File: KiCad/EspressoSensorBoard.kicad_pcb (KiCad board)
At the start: 2 copper layers, 100.4 x 22 mm, 16 parts, among them IC1 FDC1004DGSR, J1 Display, J2 MAX31855 (Temperature), J3 Screw_Terminal_01x02, J5 Pressure_Sensor, J7 Arduino_Nano_v3_Left, J8 Arduino_Nano_v3_Right, J9 Water_Level_Electrodes

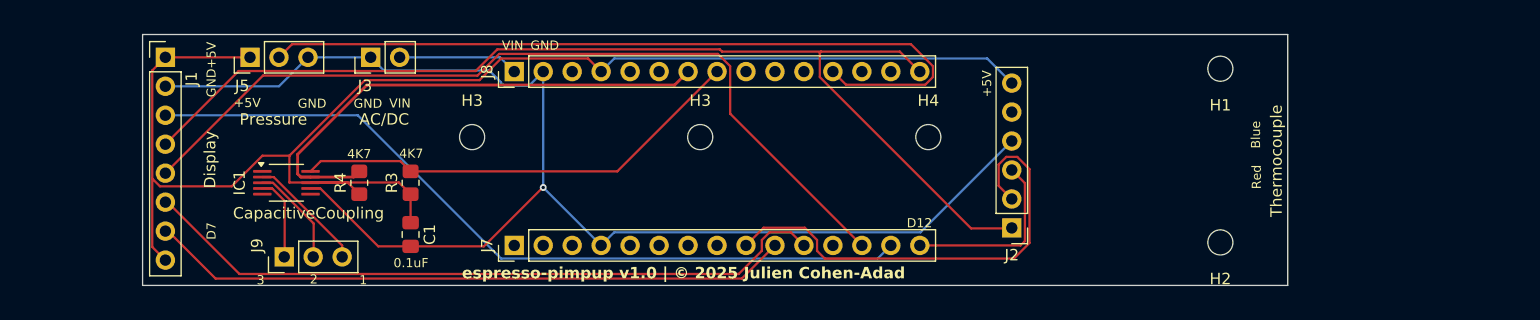
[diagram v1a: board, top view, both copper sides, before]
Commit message: Updated PCB and Arduino code
- Swapped D7 with D9 for easier routing
- Removed connection to RST on the Display (should work without it)
- Replaced connectors, notably using JST GH1.25mm for the display. https://github.com/jcohenadad/espresso-pimpup/issues/28
- Changed 3D model for Arduino. https://github.com/jcohenadad/espresso-pimpup/issues/44
- Connected pin to shielding on FDC1004. https://github.com/jcohenadad/espresso-pimpup/issues/41
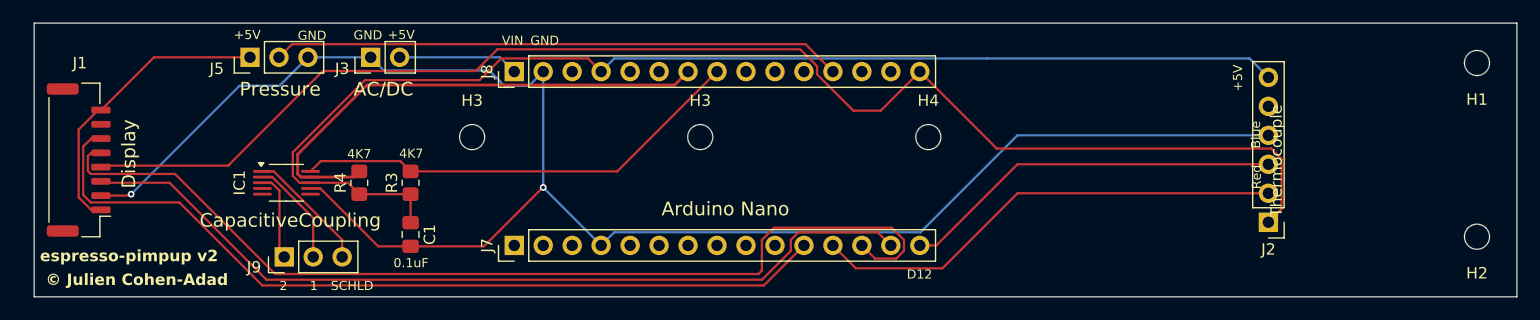
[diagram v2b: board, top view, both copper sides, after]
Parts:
- J1: value Display -> GRAPHIC DISPLAY IPS - 1.69"; footprint Connector_PinHeader_2.54mm:PinHeader_1x08_P2.54mm_Vertical -> Connector_JST:JST_GH_BM08B-GHS-TBT_1x08-1MP_P1.25mm_Vertical
- moved H1 22.5 mm to (216.0, 59.5)
- moved H2 22.5 mm to (216.0, 74.7)
- moved J2 22.5 mm to (197.7, 73.5)
- moved J1 11.8 mm to (93.4, 68.0), turned to 90 degrees
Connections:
- IC1 pad 1: unconnected-(IC1-SHLD1-Pad1) -> Net-(IC1-SHLD1)
- IC1 pad 4: Net-(IC1-CIN3) -> unconnected-(IC1-CIN3-Pad4)
- J1 pad 7: /D7 -> /RST
- J2 pad 2: /D6 -> /D9
- J7 pad 10: /D7 -> unconnected-(J7-Pin_10-Pad10)
- J7 pad 9: /D6 -> unconnected-(J7-Pin_9-Pad9)
- J9 pad 1: Net-(IC1-CIN3) -> Net-(IC1-CIN2)
- J9 pad 2: Net-(IC1-CIN2) -> Net-(IC1-CIN1)
- J9 pad 3: Net-(IC1-CIN1) -> Net-(IC1-SHLD1)
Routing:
- net /D7: track 56.7 -> 0.00 mm
- net /D9: track 0.00 -> 41.7 mm
- net /D6: track 41.1 -> 0.00 mm
- net GND: track 117.6 -> 150.0 mm, vias 1 -> 2
- net /CLK: track 95.6 -> 121.1 mm
- net /A0: track 69.1 -> 50.0 mm
- net /D12: track 16.1 -> 33.5 mm
- net /D8: track 61.4 -> 74.0 mm
- net /CS: track 74.8 -> 87.0 mm
- net Net-(IC1-SHLD1): track 0.00 -> 11.0 mm
- net Net-(IC1-CIN3): track 7.82 -> 0.00 mm
- net /D11: track 69.3 -> 75.6 mm
- net +5V: track 128.9 -> 132.1 mm
- net Net-(IC1-CIN1): track 11.0 -> 9.36 mm
- net Net-(IC1-CIN2): track 9.41 -> 7.77 mm
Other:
- board size 100.4 x 22 mm -> 130 x 24 mm
- board text added: "Arduino Nano"
- board text added: "SCHLD"
- board text added: "espresso-pimpup v2"
- board text added: "© Julien Cohen-Adad"
- board text removed: "3"
- board text removed: "D7"
- board text removed: "espresso-pimpup v1.0 | © 2025 Julien Cohen-Adad"

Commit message: Minor modifs on the Kicad PCD
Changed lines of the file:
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@@
 		(start 112.875488 69.5)
 		(end 113.725 69.5)
-		(width 0.25)
+		(width 0.2)
 		(layer "F.Cu")
 		(net 34)
@@
 		(start 145.652288 61.429084)
 		(end 118.67337 61.429084)
-		(width 0.25)
+		(width 0.2)
 		(layer "F.Cu")
 		(net 34)
@@
 		(start 146.828288 60.253084)
 		(end 145.652288 61.429084)
-		(width 0.25)
+		(width 0.2)
 		(layer "F.Cu")
 		(net 34)
@@
 		(start 112.5965 67.505954)
 		(end 112.5965 69.221012)
-		(width 0.25)
+		(width 0.2)
 		(layer "F.Cu")
 		(net 34)
@@
 		(start 117.5 69.5)
 		(end 113.725 69.5)
-		(width 0.25)
+		(width 0.2)
 		(layer "F.Cu")
 		(net 34)
@@
 		(start 118.67337 61.429084)
 		(end 112.5965 67.505954)
-		(width 0.25)
+		(width 0.2)
 		(layer "F.Cu")
 		(net 34)
@@
 		(start 112.5965 69.221012)
 		(end 112.875488 69.5)
-		(width 0.25)
+		(width 0.2)
 		(layer "F.Cu")
 		(net 34)

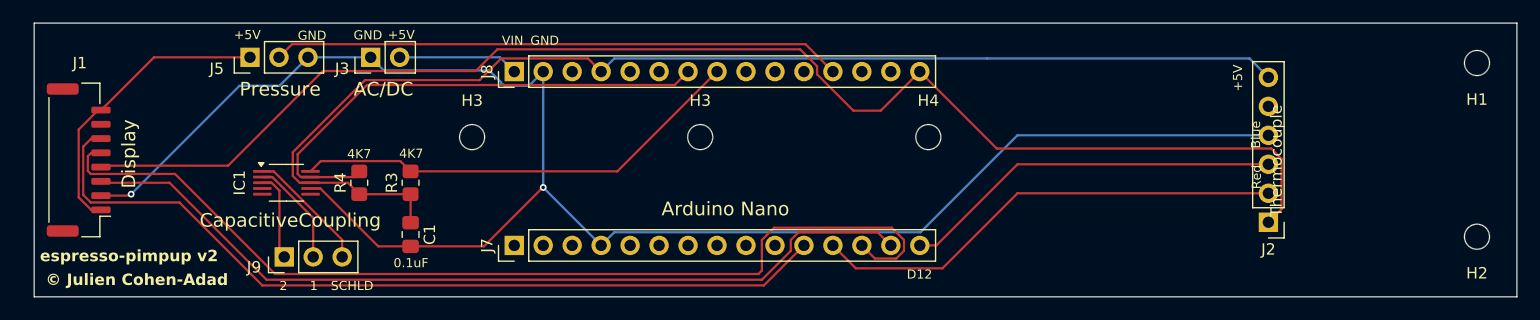
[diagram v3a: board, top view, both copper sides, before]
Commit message: Fixed missing connection
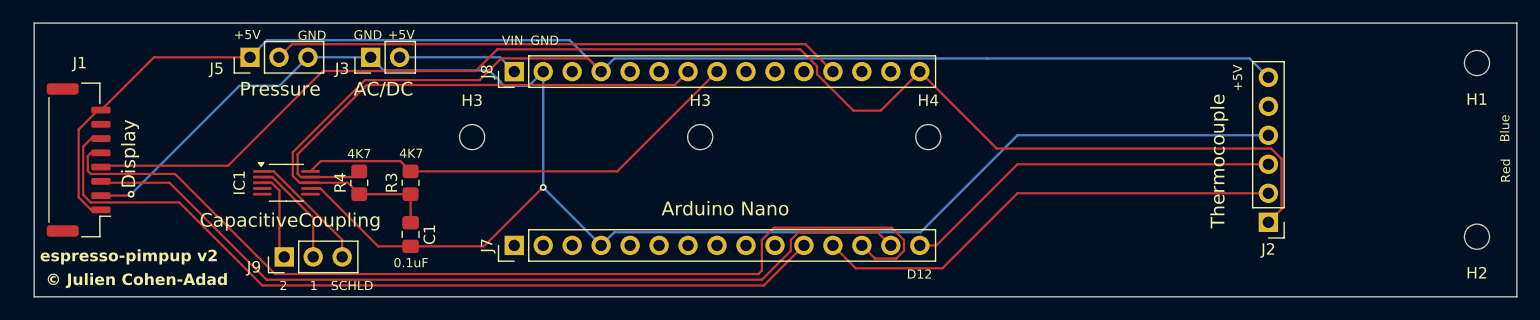
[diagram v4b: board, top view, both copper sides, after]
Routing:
- net +5V: track 132.1 -> 164.7 mm
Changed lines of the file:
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@@
 			"XgcJAQAAAHBIeykBAAAAoLItLwEAAAAwQtgrAQAAALDaBwkBAAAAcNsHCQEAAABQDf4IAQAAAHBI"
 			"eykBAAAAcEh7KQEAAABwSHspAQAAAHBIeykBAAAAMELYKwEAAABwSHspAQAAAFAN/ggBAAAA0LIt"
-			"Lw=="
+			"LwAAAAAAAAAAAAAAAAAAAAAAAAAAAAAAAAAAAAAAAAAAAAAAAAAAAAAAAAAAAAAAAAAAAAAAAAAA"
+			"AAAAAAAAAAAAAAAAAAAAAAAAAAAAAAAAAAAAAAAAAAAAAAAAAAAAAAAAAAAAAAAAAAAAAAAAAAAA"
+			"AAAAAAAAAAAAAAAAAAAAAAAAAAAAAAAAAAAAAAAAAAAAAAAAAAAAAAAAAAAAAAAAAAAAAAAAAAAA"
+			"AAAAAAAAAAAAAAAAAAAAAAAAAAAAAAAAAAAAAAAAAAAAAAAAAAAAAAAAAAAAAAAAAAAAAAAAAAAA"
+			"AAAAAAAAAAAAAAAAAAAAAAAAAAAAAAAAAAAAAAAAAAAAAAAAAAAAAAAAAAAAAAAAAAAAAAAAAAAA"
+			"AAAAAAAAAAAAAAAAAAAAAAAAAAAAAAAAAAAAAAAAAAAAAAAAAAAAAAAAAAAAAAAAAAAAAAAAAAAA"
+			"AAAAAAAAAAAAAAAAAAAAAAAAAAAAAAAAAAAAAAAAAAAAAAAAAAAAAAAAAAAAAAAAAAAAAAAAAAAA"
+			"AAAAAAAAAAAAAAAAAAAAAAAAAAAAAAAAAAAAAAAAAAAAAAAAAAAAAAAAAAAAAAAAAAAAAAAAAAAA"
+			"AAAAAAAAAAAAAAAAAAAAAAAAAAAAAAAAAAAAAAAAAAAAAAAAAAAAAAAAAAAAAAAAAAAAAAAAAAAA"
+			"AAAAAAAAAAAAAAAAAAAAAAAAAAAAAAAAAAAAAAAAAAAAAAAAAAAAAAAAAAAAAAAAAAAAAAAAAAAA"
+			"AAAAAAAAAAAAAAAAAAAAAAAAAAAAAAAAAAAAAAAAAAAAAAAAAAAAAAAAAAAAAAAAAAAAAAAAAAAA"
+			"AAAAAAAAAAAAAAAAAAAAAAAAAAAAAAAAAAAAAAAAAAAAAAAAAAAAAAAAAAAAAAAAAAAAAAAAAAAA"
+			"AAAAAAAAAAAAAAAAAAAAAAAAAAAAAAAAAAAAAAAAAAAAAAAAAAAAAAAAAAAAAAAAAAAAAAAAAAAA"
+			"AAAAAAAAAAAAAAAAAAAAAAAAAAAAAAAAAAAAAAAAAAAAAAAAAAAAAAAAAAAAAAAAAAAAAAAAAAAA"
+			"AAAAAAAAAAAAAAAAAAAAAAAAAAAAAAAAAAAAAAAAAAAAAAAAAAAAAAAAAAAAAAAAAAAAAAAAAAAA"
+			"AAAAAAAAAAAAAAAAAAAAAAAAAAAAAAAAAAAAAAAAAAAAAAAAAAAAAAAAAAAAAAAAAAAAAAAAAAAA"
+			"AAAAAAAAAAAAAAAAAAAAAAAAAAAAAAAAAAAAAAAAAAAAAAAAAAAAAAAAAAAAAAAAAAAAAAAAAAAA"
+			"AAAAAAAAAAAAAAAAAAAAAAAAAAAAAAAAAAAAAAAAAAAAAAAAAAAAAAAAAAAAAAAAAAAAAAAAAAAA"
+			"AA=="
 		)
 	)
@@
 			"AAAAUgAAAGYAAABiAAAATwAAAHoAAABEAAAAQQAAADUAAABPAAAAWgAAAGwAAABSAAAAUgAAAGsA"
 			"AABVAAAASAAAADYAAAA1AAAARQAAAGoAAABSAAAAKwAAAGkAAAAwAAAAWAAAAE0AAABxAAAARgAA"
-			"AFEAAABmAAAAbwAAAEgAAABoAAAAMQ=="
+			"AFEAAABmAAAAbwAAAEgAAABoAAAAMQAAAAAAAAAAAAAAAAAAAAAAAAAAAAAAAAAAAAAAAAAAAAAA"
+			"AAAAAAAAAAAAAAAAAAAAAAAAAAAAAAAAAAAAAAAAAAAAAAAAAAAAAAAAAAAAAAAAAAAAAAAAAAAA"
+			"AAAAAAAAAAAAAAAAAAAAAAAAAAAAAAAAAAAAAAAAAAAAAAAAAAAAAAAAAAAAAAAAAAAAAAAAAAAA"
+			"AAAAAAAAAAAAAAAAAAAAAAAAAAAAAAAAAAAAAAAAAAAAAAAAAAAAAAAAAAAAAAAAAAAAAAAAAAAA"
+			"AAAAAAAAAAAAAAAAAAAAAAAAAAAAAAAAAAAAAAAAAAAAAAAAAAAAAAAAAAAAAAAAAAAAAAAAAAAA"
+			"AAAAAAAAAAAAAAAAAAAAAAAAAAAAAAAAAAAAAAAAAAAAAAAAAAAAAAAAAAAAAAAAAAAAAAAAAAAA"
+			"AAAAAAAAAAAAAAAAAAAAAAAAAAAAAAAAAAAAAAAAAAAAAAAAAAAAAAAAAAAAAAAAAAAAAAAAAAAA"
+			"AAAAAAAAAAAAAAAAAAAAAAAAAAAAAAAAAAAAAAAAAAAAAAAAAAAAAAAAAAAAAAAAAAAAAAAAAAAA"
+			"AAAAAAAAAAAAAAAAAAAAAAAAAAAAAAAAAAAAAAAAAAAAAAAAAAAAAAAAAAAAAAAAAAAAAAAAAAAA"
+			"AAAAAAAAAAAAAAAAAAAAAAAAAAAAAAAAAAAAAAAAAAAAAAAAAAAAAAAAAAAAAAAAAAAAAAAAAAAA"
+			"AAAAAAAAAAAAAAAAAAAAAAAAAAAAAAAAAAAAAAAAAAAAAAAAAAAAAAAAAAAAAAAAAAAAAAAAAAAA"
+			"AAAAAAAAAAAAAAAAAAAAAAAAAAAAAAAAAAAAAAAAAAAAAAAAAAAAAAAAAAAAAAAAAAAAAAAAAAAA"
+			"AAAAAAAAAAAAAAAAAAAAAAAAAAAAAAAAAAAAAAAAAAAAAAAAAAAAAAAAAAAAAAAAAAAAAAAAAAAA"
+			"AAAAAAAAAAAAAAAAAAAAAAAAAAAAAAAAAAAAAAAAAAAAAAAAAAAAAAAAAAAAAAAAAAAAAAAAAAAA"
+			"AAAAAAAAAAAAAAAAAAAAAAAAAAAAAAAAAAAAAAAAAAAAAAAAAAAAAAAAAAAAAAAAAAAAAAAAAAAA"
+			"AAAAAAAAAAAAAAAAAAAAAAAAAAAAAAAAAAAAAAAAAAAAAAAAAAAAAAAAAAAAAAAAAAAAAAAAAAAA"
+			"AAAAAAAAAAAAAAAAAAAAAAAAAAAAAAAAAAAAAAAAAAAAAAAAAAAAAAAAAAAAAAAAAAAAAAAAAAAA"
+			"AAAAAAAAAAAAAAAAAAAAAAAAAAAAAAAAAAAAAAAAAAAAAAAAAAAAAAAAAAAAAAAAAAAAAAAAAAAA"
+			"AAAAAAAAAAAAAAAAAAAAAAAAAAAAAA=="
 		)
 	)
@@
 			"AAICAwADAgAA/v8AAP//AAD+/v4AxcbCAIaKhQDGycYAMjQyAHV2dwBFQUgA/AD9AAUABgD8APwA"
 			"BAAEAP0A+wD+//0ABgEFAPoA+wAEAAQA/wD/APwA/QD2+PYAoaOiAIGGhQD68/AAOlJQABAaGADW"
-			"2toAGxgcAC8qLQAfGR0AFA=="
+			"2toAGxgcAC8qLQAfGR0AFADe4eAA+v38AMjKyQAJCgkALi0tANTT0gAB//8ABAMCAOfm5gAICAkA"
+			"BAQEAAEBAAD+//4AAwUDAPL18wD9AP8A/wQCABwgHwD5+/oAAwQEAAUEBAD9+fkAAf3/AAQAAQD4"
+			"9/QABAMAAA4QDAAFBQQAAAABAPz4/gD19fgAFxgaABcUFADy6+oAGBgWAAgOCwDh4+MA8fHzAA4O"
+			"DgDr6+gA/v7+AAMEBgD//wAABQUEAPf49gD6+/oADQ0MAP8A/gDs7OwADAwLAAD+/wARERIADg0N"
+			"AOTj5QD7+vsAIyMkAAQGBwDe4uIA/wIDAAgLCwAAAwEA+v77AP4B/QABAv0AAAIAAAUHCQAFBgoA"
+			"BQYLAAcGCwAEAwYABQIDAPj29AAI/v4AW0tLAEUxQwEAAAAAAAAAAAAAAAAAAAAAAAAAAAAAAAAA"
+			"AAAAAAAAAAAAAAAAAAAAAAAAAAAAAAAAAAAAAAAAAAAAAAAAAAAAAAAAAAAAAAAAAAAAAAAAAAAA"
+			"AAAAAAAAAAAAAAAAAAAAAAAAAAAAAAAAAAAAAAAAAAAAAAAAAAAAAAAAAAAAAAAAAAAAAAAAAAAA"
+			"AAAAAAAAAAAAAAAAAAAAAAAAAAAAAAAAAAAAAAAAAAAAAAAAAAAAAAAAAAAAAQAAAAAAAAAAAAAA"
+			"AAAAAAAAAAAAAAAAAAAAAAAAAAAAAAAAAAAAAAAAAAAAAAAAAAAAAAAAAAAAAAAAAAAAAAAAAAAA"
+			"AAAAAAAAAAAAAAAAAAAAANnS2v/z9vcABg0MAPv+/gD+/P4A/Pv6AAH9/AACAAAA+vz7AP7//wD7"
+			"/fwA+/z8AAQEAwD9/v0ABQUEAPn5+AD49/YAAgIBAPz8/AAICAcAAwQEAAUGBAAICAcAAAABAAMA"
+			"BwD8/AAA+vn8AP7+/gD/Af4AAwUDAPr6+QD9/f0A+vr7AP7+/wD6+vkA/v37AAIB/QD++/sABAED"
+			"AP7//wD6/fwA+/z7AAMCAwAMCwoAAP/8APP18gAQFRIA8/TzAPf29gAA/gAA//z+AAYGBwAGCQkA"
+			"BQYHAAYDBQAKCQsADg4PAAUFBgDj4+QAAwMEAAoJCgAJCgoA8PHyAP///wABAQAAAQEAAPf39gDv"
+			"8O4AAQEAABAREAAAAQAAAf8AAAD7/wAB/gAABQUFAP7+/QD8Af0A9fb2APT19QAA/wEA8u3yAPz6"
+			"+wAJCgcA+fv3APb69QD///0AAP4AAAQFAwANEAwA/f/9AP8BBAAMCg0AAv8CAAkJCQD/Av8ABgoI"
+			"AAkLDAACAQIA+PT3ABMVEwD5APgA7/HuAAUCAwD//f8AAQAAAPP09QAGBwgAAgQDAP3+/wD9/f0A"
+			"CAcGAAMAAQAD/gAA//79AA=="
 		)
 	)
@@
 	)
 	(gr_text "Blue"
-		(at 197.077899 67 90)
+		(at 218.931531 66.439593 90)
 		(layer "F.SilkS")
 		(effects
@@
 	)
 	(gr_text "Thermocouple"
-		(at 199 73 90)
+		(at 194 74 90)
 		(layer "F.SilkS")
 		(effects
 			(font
-				(size 1 1)
-				(thickness 0.1)
+				(size 1.2 1.2)
+				(thickness 0.15)
 			)
 			(justify left bottom)
@@
 	)
 	(gr_text "Red"
-		(at 197.146368 70.560407 90)
+		(at 219 70 90)
 		(layer "F.SilkS")
 		(effects
@@
 	)
 	(segment
+		(start 139.208288 60.253084)
+		(end 136.455204 57.5)
+		(width 0.2)
+		(layer "B.Cu")
+		(net 2)
+	)
+	(segment
+		(start 136.455204 57.5)
+		(end 109.92 57.5)
+		(width 0.2)
+		(layer "B.Cu")
+		(net 2)
+	)
+	(segment
 		(start 196.054084 59.102084)
 		(end 173.054084 59.102084)
@@
 		(width 0.2)
 		(layer "B.Cu")
+		(net 2)
+	)
+	(segment
+		(start 109.92 57.5)
+		(end 108.42 59)
+		(width 0.2)
+		(layer "B.Cu")

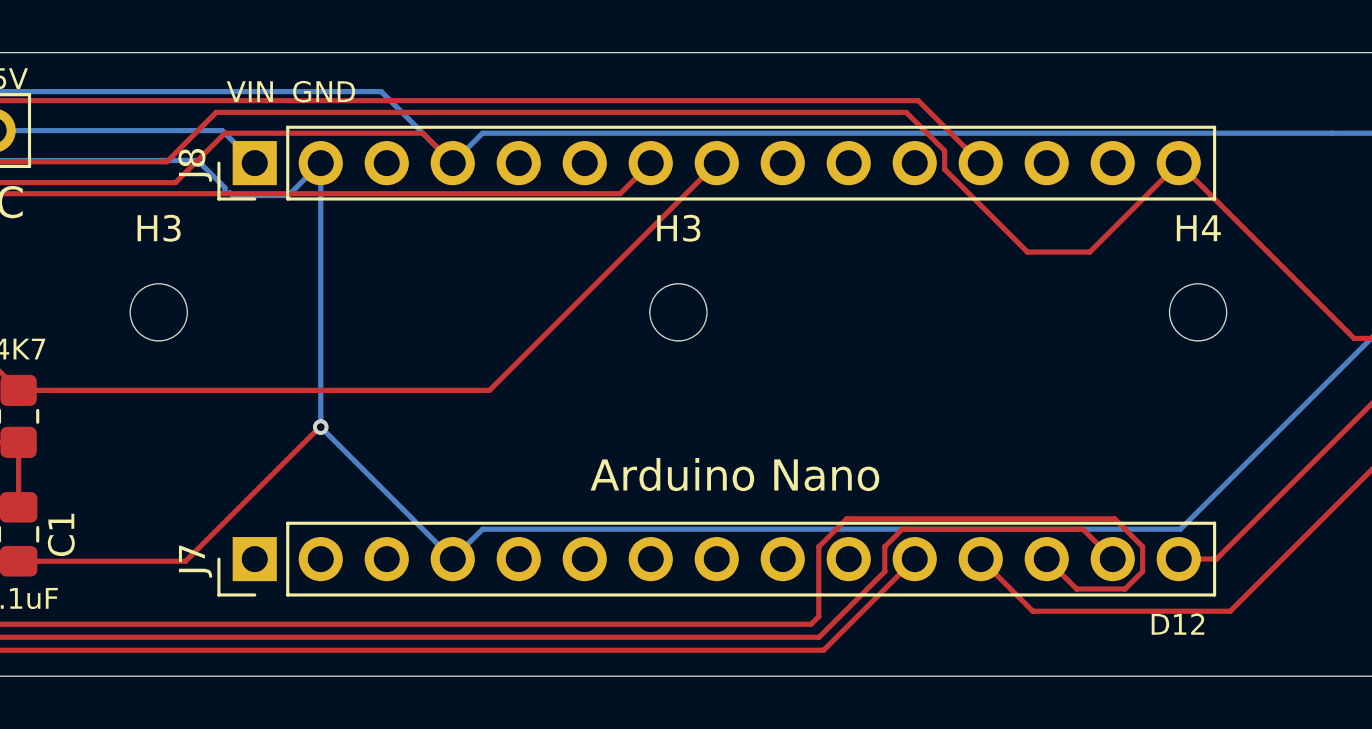
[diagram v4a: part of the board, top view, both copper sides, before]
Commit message: Fixed arduino connector
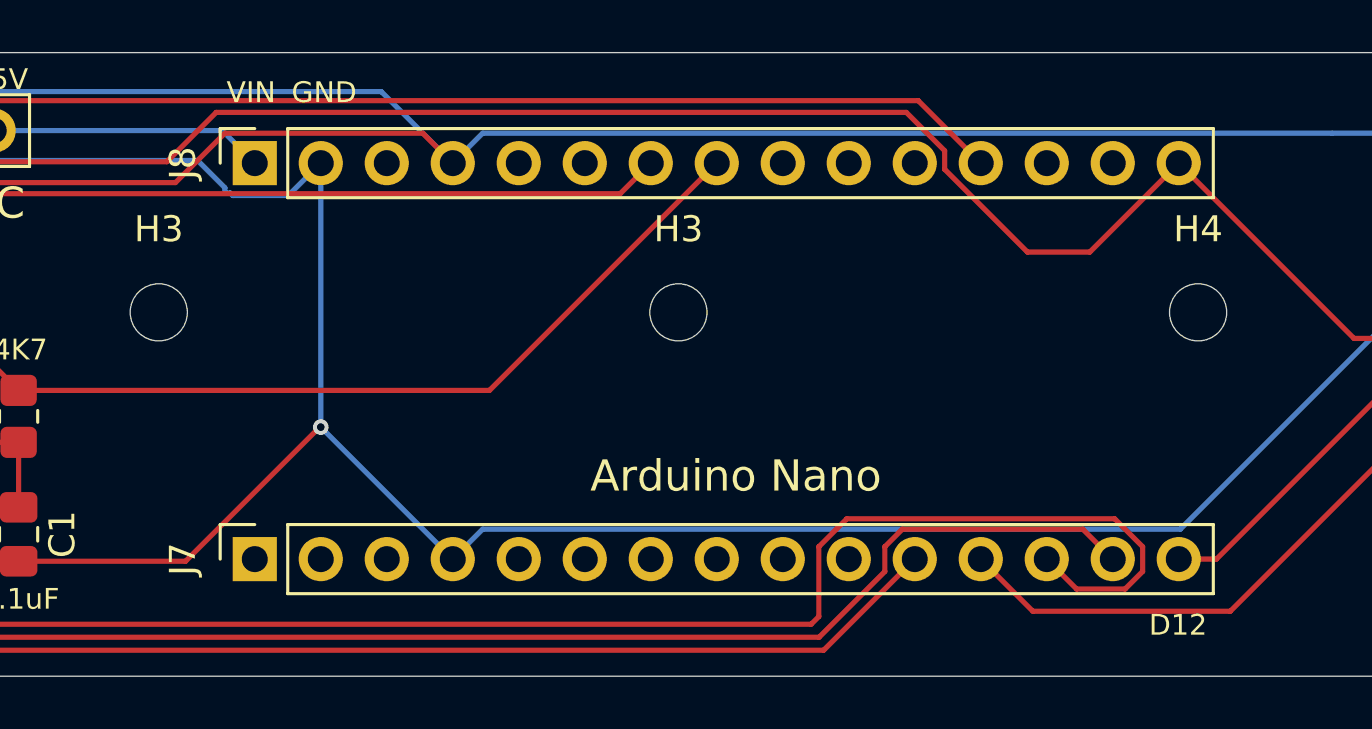
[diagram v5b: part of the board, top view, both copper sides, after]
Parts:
- J7, J8: footprint Connector_PinHeader_2.54mm:PinHeader_1x15_P2.54mm_Vertical -> Connector_PinSocket_2.54mm:PinSocket_1x15_P2.54mm_Vertical
